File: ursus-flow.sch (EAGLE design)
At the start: 61 parts

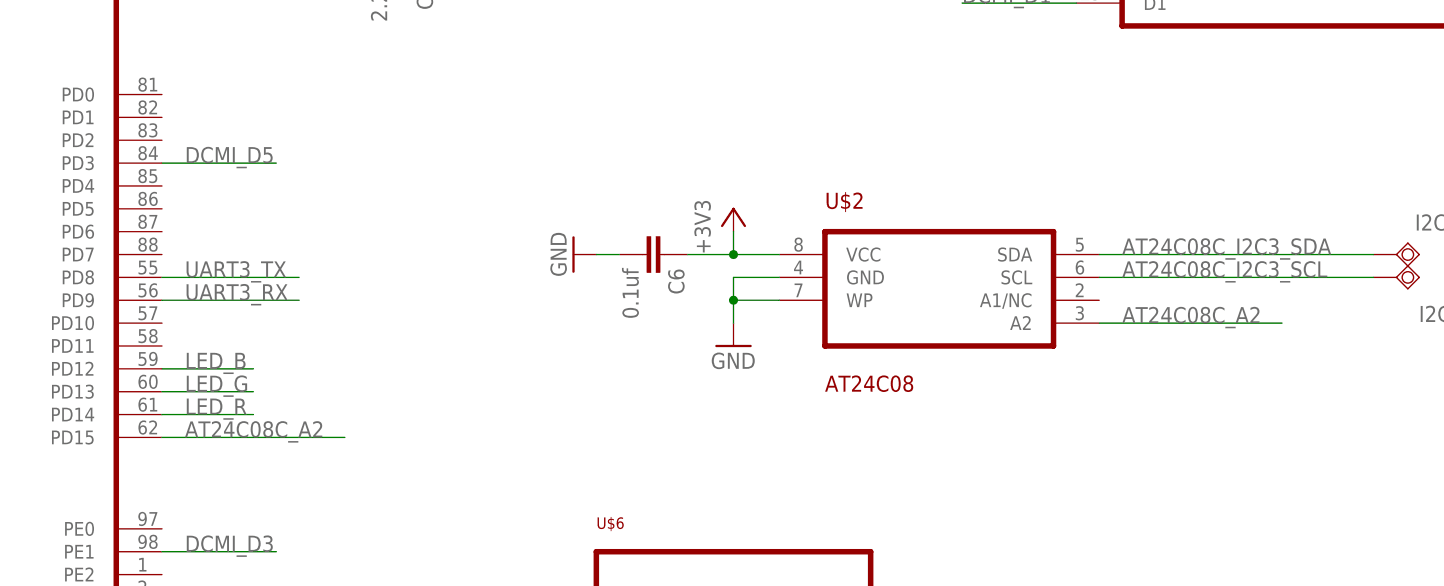
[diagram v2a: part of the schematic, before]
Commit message: Finish PCB layout
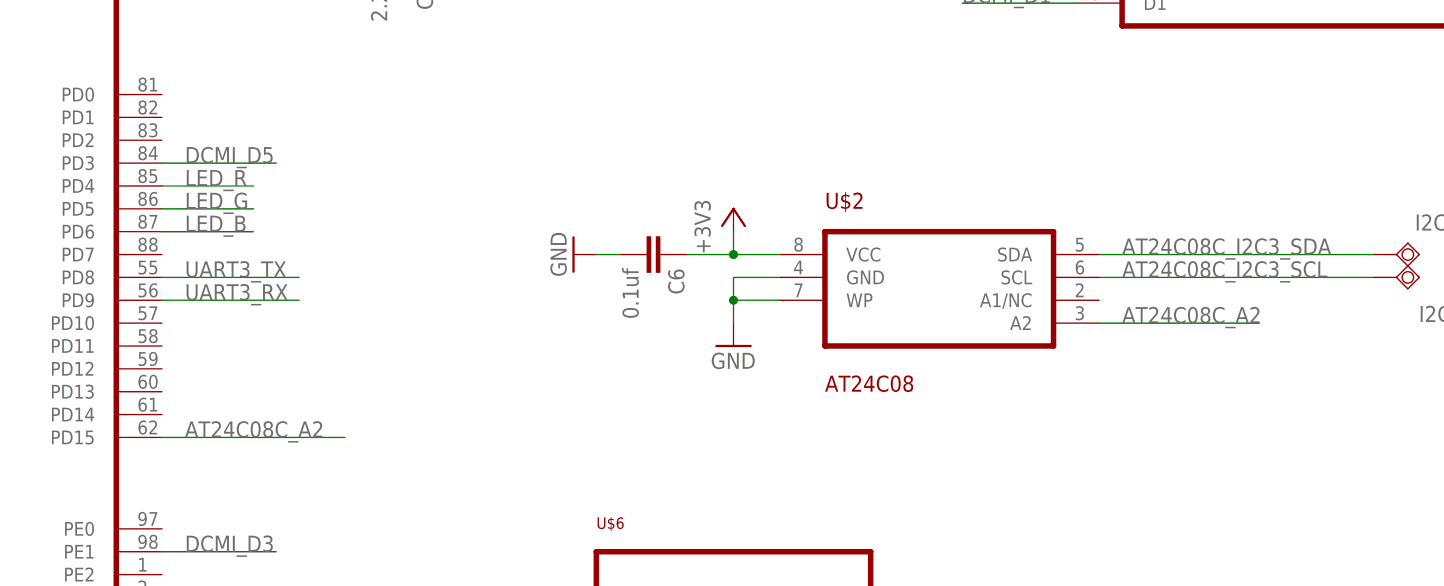
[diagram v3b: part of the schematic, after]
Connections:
- net LED_B: now also U$1.PD6; no longer U$1.PD12
- net LED_G: now also U$1.PD5; no longer U$1.PD13
- net LED_R: now also U$1.PD4; no longer U$1.PD14
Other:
- note removed: "MPU9250(Breakboard Module)"
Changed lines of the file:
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@@
 <part name="U$9" library="M3_HOLE" deviceset="M3_HOLE" device=""/>
 <part name="U$10" library="M3_HOLE" deviceset="M3_HOLE" device=""/>
-<part name="U$11" library="MPU9250_BREAKOUT" deviceset="MPU9250_BREAKOUT" device=""/>
 <part name="+3V9" library="supply1" deviceset="+3V3" device=""/>
 <part name="GND8" library="supply1" deviceset="GND" device=""/>
+<part name="U$11" library="MPU9250_BREAKOUT" deviceset="MPU9250_BREAKOUT" device=""/>
 </parts>
 <sheets>
@@
 <text x="-76.2" y="213.36" size="1.778" layer="98">UART2</text>
 <text x="-76.2" y="175.26" size="1.778" layer="98">Lidar</text>
-<text x="121.92" y="17.78" size="1.778" layer="98">MPU9250(Breakboard Module)</text>
 <text x="68.58" y="71.12" size="1.778" layer="98">MT9V034(Breakboard Module)</text>
 <text x="10.16" y="213.36" size="1.778" layer="98">Power from UBEC (5V)</text>
@@
 <instance part="U$9" gate="G$1" x="30.48" y="-58.42"/>
 <instance part="U$10" gate="G$1" x="43.18" y="-58.42"/>
-<instance part="U$11" gate="G$1" x="129.54" y="10.16" rot="R180"/>
 <instance part="+3V9" gate="G$1" x="175.26" y="0" rot="R270"/>
 <instance part="GND8" gate="1" x="180.34" y="2.54" rot="R90"/>
+<instance part="U$11" gate="G$1" x="129.54" y="10.16" rot="R180"/>
 </instances>
 <busses>
@@
 <net name="LED_B" class="0">
 <segment>
-<pinref part="U$1" gate="G$1" pin="PD12"/>
-<wire x1="-38.1" y1="-2.54" x2="-27.94" y2="-2.54" width="0.1524" layer="91"/>
-<label x="-35.56" y="-2.54" size="1.778" layer="95"/>
-</segment>
-<segment>
 <wire x1="116.84" y1="119.38" x2="127" y2="119.38" width="0.1524" layer="91"/>
 <label x="116.84" y="119.38" size="1.778" layer="95"/>
 <pinref part="LED3" gate="G$1" pin="A"/>
 </segment>
+<segment>
+<wire x1="-38.1" y1="12.7" x2="-27.94" y2="12.7" width="0.1524" layer="91"/>
+<label x="-35.56" y="12.7" size="1.778" layer="95"/>
+<pinref part="U$1" gate="G$1" pin="PD6"/>
+</segment>
 </net>
 <net name="LED_G" class="0">
-<segment>
-<pinref part="U$1" gate="G$1" pin="PD13"/>
-<wire x1="-38.1" y1="-5.08" x2="-27.94" y2="-5.08" width="0.1524" layer="91"/>
-<label x="-35.56" y="-5.08" size="1.778" layer="95"/>
-</segment>
 <segment>
 <wire x1="116.84" y1="109.22" x2="127" y2="109.22" width="0.1524" layer="91"/>
@@
 <pinref part="LED2" gate="G$1" pin="A"/>
 </segment>
+<segment>
+<wire x1="-38.1" y1="15.24" x2="-27.94" y2="15.24" width="0.1524" layer="91"/>
+<label x="-35.56" y="15.24" size="1.778" layer="95"/>
+<pinref part="U$1" gate="G$1" pin="PD5"/>
+</segment>
 </net>
 <net name="LED_R" class="0">
-<segment>
-<pinref part="U$1" gate="G$1" pin="PD14"/>
-<wire x1="-38.1" y1="-7.62" x2="-27.94" y2="-7.62" width="0.1524" layer="91"/>
-<label x="-35.56" y="-7.62" size="1.778" layer="95"/>
-</segment>
 <segment>
 <wire x1="116.84" y1="99.06" x2="127" y2="99.06" width="0.1524" layer="91"/>
@@
 <pinref part="LED1" gate="G$1" pin="A"/>
 </segment>
+<segment>
+<wire x1="-38.1" y1="17.78" x2="-27.94" y2="17.78" width="0.1524" layer="91"/>
+<label x="-35.56" y="17.78" size="1.778" layer="95"/>
+<pinref part="U$1" gate="G$1" pin="PD4"/>
+</segment>
 </net>
 <net name="AT24C08C_A2" class="0">
 <segment>
-<wire x1="86.36" y1="2.54" x2="66.04" y2="2.54" width="0.1524" layer="91"/>
+<wire x1="83.82" y1="2.54" x2="66.04" y2="2.54" width="0.1524" layer="91"/>
 <pinref part="U$2" gate="G$1" pin="A2"/>
 <label x="68.58" y="2.54" size="1.778" layer="95"/>

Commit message: Do circuit final check
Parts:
- removed C19: 100uf/10V, rcl:CPOL-USB/3528-21W
- removed U$10, U$7, U$8, U$9: M3_HOLE, M3_HOLE:M3_HOLE
- added C18: 100uf/10V, rcl:CPOL-USC/6032-28R
- added U$12, U$13, U$14, U$15: M3_HOLE, M3_HOLE:M3_HOLE
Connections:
- net +5V: now also C18.+; no longer C19.+
- net GND: now also C18.-; no longer C19.-, U$3.GND3, U$3.GND4
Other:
- moved on the sheet: U$6
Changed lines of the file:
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@@
 <part name="[ST-LINK]" library="con-lstb" deviceset="MA04-1" device="" value="stlink_connector"/>
 <part name="GND11" library="supply1" deviceset="GND" device=""/>
-<part name="U$3" library="usb_mirco_b" deviceset="MICRO-USB-RECEPTACLE" device="47589-0001"/>
 <part name="GND12" library="supply1" deviceset="GND" device=""/>
 <part name="GND14" library="supply1" deviceset="GND" device=""/>
@@
 <part name="GND13" library="supply1" deviceset="GND" device=""/>
 <part name="R18" library="resistor" deviceset="R-EU_" device="R0805W" value="1k"/>
-<part name="C19" library="rcl" deviceset="CPOL-US" device="B/3528-21W" value="100uf/10V"/>
 <part name="C20" library="rcl" deviceset="CPOL-US" device="B/3528-21W" value="100uf/10V"/>
 <part name="GND30" library="supply1" deviceset="GND" device=""/>
@@
 <part name="I2C3_SDA" library="testpad" deviceset="TPSQ" device="TP20SQ"/>
 <part name="I2C3_SCL" library="testpad" deviceset="TPSQ" device="TP20SQ"/>
-<part name="U$6" library="LIDAR_MOUNT" deviceset="LIDAR_MOUNT" device=""/>
-<part name="U$7" library="M3_HOLE" deviceset="M3_HOLE" device=""/>
-<part name="U$8" library="M3_HOLE" deviceset="M3_HOLE" device=""/>
-<part name="U$9" library="M3_HOLE" deviceset="M3_HOLE" device=""/>
-<part name="U$10" library="M3_HOLE" deviceset="M3_HOLE" device=""/>
 <part name="+3V9" library="supply1" deviceset="+3V3" device=""/>
 <part name="GND8" library="supply1" deviceset="GND" device=""/>
 <part name="U$11" library="MPU9250_BREAKOUT" deviceset="MPU9250_BREAKOUT" device=""/>
+<part name="U$6" library="LIDAR_MOUNT" deviceset="LIDAR_MOUNT" device=""/>
+<part name="U$3" library="usb_mirco_b" deviceset="MICRO-USB-RECEPTACLE" device="47589-0001"/>
+<part name="C18" library="rcl" deviceset="CPOL-US" device="C/6032-28R" value="100uf/10V"/>
+<part name="U$12" library="M3_HOLE" deviceset="M3_HOLE" device=""/>
+<part name="U$13" library="M3_HOLE" deviceset="M3_HOLE" device=""/>
+<part name="U$14" library="M3_HOLE" deviceset="M3_HOLE" device=""/>
+<part name="U$15" library="M3_HOLE" deviceset="M3_HOLE" device=""/>
 </parts>
 <sheets>
@@
 <instance part="[ST-LINK]" gate="1" x="60.96" y="114.3"/>
 <instance part="GND11" gate="1" x="71.12" y="101.6"/>
-<instance part="U$3" gate="G$1" x="17.78" y="167.64" rot="R180"/>
 <instance part="GND12" gate="1" x="30.48" y="180.34" rot="R180"/>
 <instance part="GND14" gate="1" x="-111.76" y="195.58"/>
@@
 <instance part="GND13" gate="1" x="7.62" y="10.16" rot="R270"/>
 <instance part="R18" gate="G$1" x="-139.7" y="53.34"/>
-<instance part="C19" gate="G$1" x="48.26" y="203.2"/>
 <instance part="C20" gate="G$1" x="114.3" y="170.18"/>
 <instance part="GND30" gate="1" x="48.26" y="193.04"/>
@@
 <attribute name="TP_SIGNAL_NAME" x="100.33" y="10.16" size="1.778" layer="97" rot="R90"/>
 </instance>
-<instance part="U$6" gate="G$1" x="25.4" y="-30.48"/>
-<instance part="U$7" gate="G$1" x="5.08" y="-58.42"/>
-<instance part="U$8" gate="G$1" x="17.78" y="-58.42"/>
-<instance part="U$9" gate="G$1" x="30.48" y="-58.42"/>
-<instance part="U$10" gate="G$1" x="43.18" y="-58.42"/>
 <instance part="+3V9" gate="G$1" x="175.26" y="0" rot="R270"/>
 <instance part="GND8" gate="1" x="180.34" y="2.54" rot="R90"/>
 <instance part="U$11" gate="G$1" x="129.54" y="10.16" rot="R180"/>
+<instance part="U$6" gate="G$1" x="22.86" y="-30.48"/>
+<instance part="U$3" gate="G$1" x="17.78" y="167.64" rot="R180"/>
+<instance part="C18" gate="G$1" x="48.26" y="203.2"/>
+<instance part="U$12" gate="G$1" x="5.08" y="-63.5"/>
+<instance part="U$13" gate="G$1" x="17.78" y="-63.5"/>
+<instance part="U$14" gate="G$1" x="30.48" y="-63.5"/>
+<instance part="U$15" gate="G$1" x="43.18" y="-63.5"/>
 </instances>
 <busses>
@@
 </segment>
 <segment>
-<pinref part="U$3" gate="G$1" pin="5"/>
 <pinref part="GND12" gate="1" pin="GND"/>
 <wire x1="22.86" y1="172.72" x2="25.4" y2="172.72" width="0.1524" layer="91"/>
 <wire x1="25.4" y1="172.72" x2="30.48" y2="172.72" width="0.1524" layer="91"/>
 <wire x1="30.48" y1="172.72" x2="30.48" y2="177.8" width="0.1524" layer="91"/>
-<pinref part="U$3" gate="G$1" pin="GND4"/>
-<wire x1="12.7" y1="180.34" x2="12.7" y2="182.88" width="0.1524" layer="91"/>
-<wire x1="12.7" y1="182.88" x2="15.24" y2="182.88" width="0.1524" layer="91"/>
-<pinref part="U$3" gate="G$1" pin="GND1"/>
 <wire x1="15.24" y1="182.88" x2="17.78" y2="182.88" width="0.1524" layer="91"/>
-<wire x1="17.78" y1="182.88" x2="20.32" y2="182.88" width="0.1524" layer="91"/>
-<wire x1="20.32" y1="182.88" x2="20.32" y2="180.34" width="0.1524" layer="91"/>
-<pinref part="U$3" gate="G$1" pin="GND3"/>
 <wire x1="15.24" y1="180.34" x2="15.24" y2="182.88" width="0.1524" layer="91"/>
-<pinref part="U$3" gate="G$1" pin="GND2"/>
 <wire x1="17.78" y1="180.34" x2="17.78" y2="182.88" width="0.1524" layer="91"/>
-<wire x1="20.32" y1="182.88" x2="25.4" y2="182.88" width="0.1524" layer="91"/>
+<wire x1="17.78" y1="182.88" x2="25.4" y2="182.88" width="0.1524" layer="91"/>
 <wire x1="25.4" y1="182.88" x2="25.4" y2="172.72" width="0.1524" layer="91"/>
-<junction x="15.24" y="182.88"/>
-<junction x="20.32" y="182.88"/>
 <junction x="25.4" y="172.72"/>
 <junction x="17.78" y="182.88"/>
+<pinref part="U$3" gate="G$1" pin="5"/>
+<pinref part="U$3" gate="G$1" pin="GND1"/>
+<pinref part="U$3" gate="G$1" pin="GND2"/>
 </segment>
 <segment>
@@
 <segment>
 <pinref part="GND30" gate="1" pin="GND"/>
-<pinref part="C19" gate="G$1" pin="-"/>
 <wire x1="48.26" y1="195.58" x2="48.26" y2="198.12" width="0.1524" layer="91"/>
+<pinref part="C18" gate="G$1" pin="-"/>
 </segment>
 <segment>
@@
 <pinref part="P+1" gate="1" pin="+5V"/>
 <wire x1="40.64" y1="208.28" x2="48.26" y2="208.28" width="0.1524" layer="91"/>
-<pinref part="C19" gate="G$1" pin="+"/>
 <wire x1="48.26" y1="208.28" x2="50.8" y2="208.28" width="0.1524" layer="91"/>
 <wire x1="48.26" y1="205.74" x2="48.26" y2="208.28" width="0.1524" layer="91"/>
 <pinref part="SCHOTTKY1" gate="G$1" pin="C"/>
 <junction x="48.26" y="208.28"/>
+<pinref part="C18" gate="G$1" pin="+"/>
 </segment>
 <segment>
@@
 <net name="V_USB" class="0">
 <segment>
-<pinref part="U$3" gate="G$1" pin="1"/>
 <wire x1="22.86" y1="162.56" x2="35.56" y2="162.56" width="0.1524" layer="91"/>
 <label x="25.4" y="162.56" size="1.778" layer="95"/>
@@
 <wire x1="35.56" y1="160.02" x2="38.1" y2="160.02" width="0.1524" layer="91"/>
 <pinref part="SCHOTTKY2" gate="G$1" pin="A"/>
-</segment>
-<segment>
+<pinref part="U$3" gate="G$1" pin="1"/>
+</segment>
+<segment>

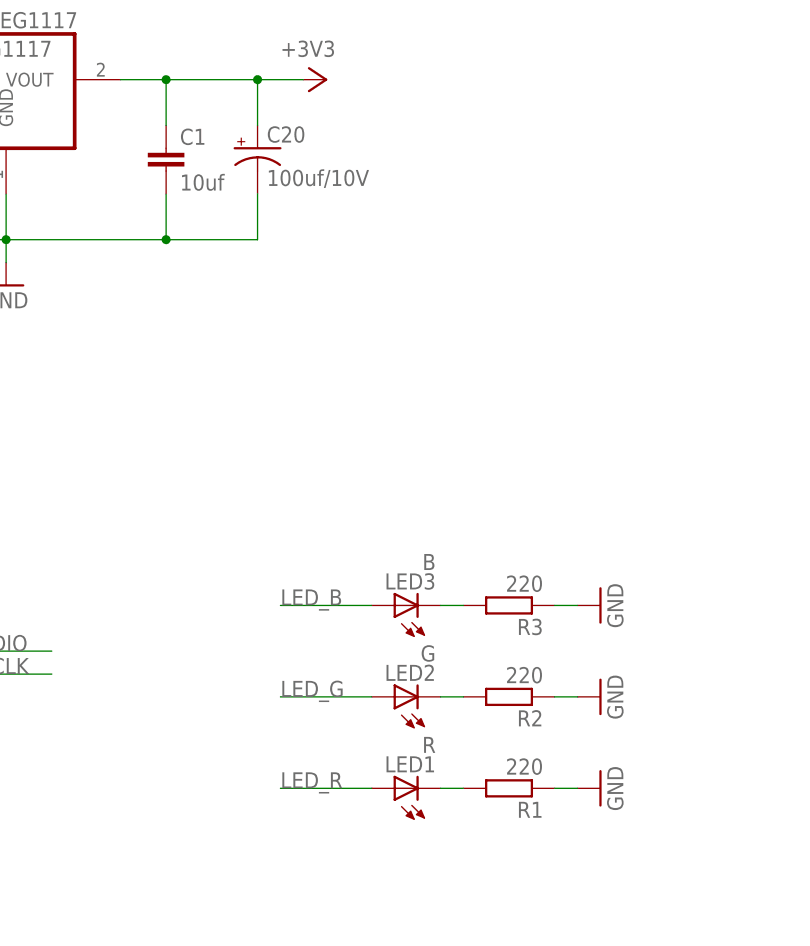
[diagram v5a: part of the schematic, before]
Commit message: Update component value
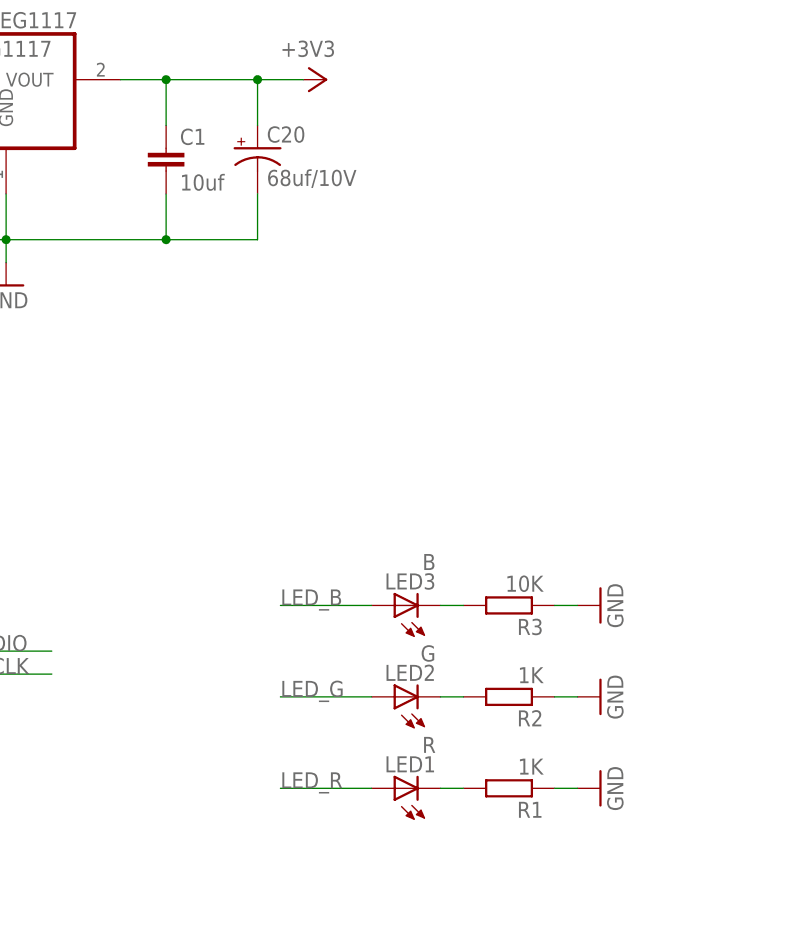
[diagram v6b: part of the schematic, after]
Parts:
- C20: value 100uf/10V -> 68uf/10V
- R1, R2: value 220 -> 1K
- R3: value 220 -> 10K
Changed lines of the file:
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@@
 <part name="LED3" library="led" deviceset="LED" device="SML0805" value="B"/>
 <part name="PWR_LED" library="led" deviceset="LED" device="SML0805" value="PWR_LED"/>
-<part name="R1" library="resistor" deviceset="R-EU_" device="R0805W" value="220"/>
-<part name="R2" library="resistor" deviceset="R-EU_" device="R0805W" value="220"/>
-<part name="R3" library="resistor" deviceset="R-EU_" device="R0805W" value="220"/>
+<part name="R1" library="resistor" deviceset="R-EU_" device="R0805W" value="1K"/>
+<part name="R2" library="resistor" deviceset="R-EU_" device="R0805W" value="1K"/>
+<part name="R3" library="resistor" deviceset="R-EU_" device="R0805W" value="10K"/>
 <part name="R4" library="resistor" deviceset="R-EU_" device="R0805W" value="220"/>
 <part name="GND1" library="supply1" deviceset="GND" device=""/>
@@
 <part name="GND13" library="supply1" deviceset="GND" device=""/>
 <part name="R18" library="resistor" deviceset="R-EU_" device="R0805W" value="1k"/>
-<part name="C20" library="rcl" deviceset="CPOL-US" device="B/3528-21W" value="100uf/10V"/>
+<part name="C20" library="rcl" deviceset="CPOL-US" device="B/3528-21W" value="68uf/10V"/>
 <part name="GND30" library="supply1" deviceset="GND" device=""/>
 <part name="[LIDAR]" library="jst-ph" deviceset="JST-PH4" device="" value="lidar_connector"/>

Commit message: Update pull up resistors for mt9v034
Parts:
- R13: value 4.7k -> no need
- R15: value 4.7k -> 1k
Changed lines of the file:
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@@
 <part name="R11" library="resistor" deviceset="R-EU_" device="R0805W" value="4.7k"/>
 <part name="R12" library="resistor" deviceset="R-EU_" device="R0805W" value="4.7k"/>
-<part name="R13" library="resistor" deviceset="R-EU_" device="R0805W" value="4.7k"/>
+<part name="R13" library="resistor" deviceset="R-EU_" device="R0805W" value="no need"/>
 <part name="R14" library="resistor" deviceset="R-EU_" device="R0805W" value="4.7k"/>
-<part name="R15" library="resistor" deviceset="R-EU_" device="R0805W" value="4.7k"/>
+<part name="R15" library="resistor" deviceset="R-EU_" device="R0805W" value="1k"/>
 <part name="R16" library="resistor" deviceset="R-EU_" device="R0805W" value="4.7k"/>
 <part name="+3V11" library="supply1" deviceset="+3V3" device=""/>
